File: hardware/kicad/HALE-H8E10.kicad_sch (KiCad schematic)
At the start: 11 parts, among them U1001 74AHCT1G125, U1002 XIAO-ESP32-S3-Plus-SMD

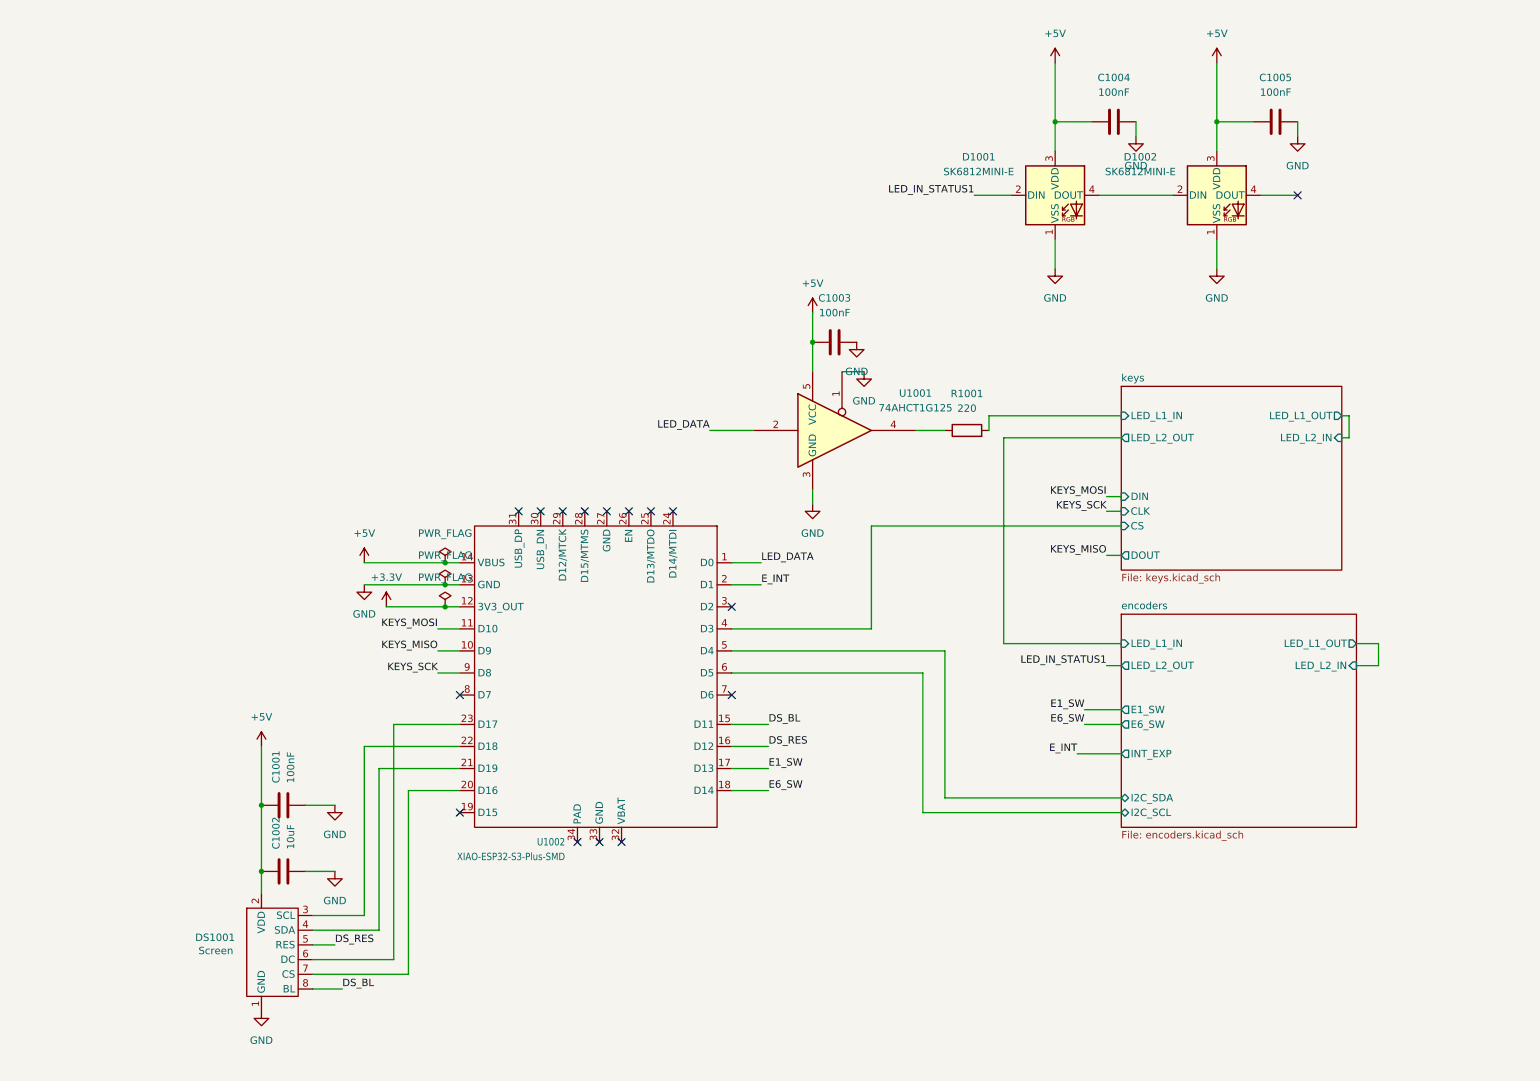
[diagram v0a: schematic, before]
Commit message: WIP checkpoint commit before spliting the 5V rail
hardware/kicad/HALE-H8E10.kicad_pcb: Manufacturing: changed the board
  outline; tenting front back → -; covering - → -; plugging - → -;
  capping - → no; filling - → no; changed the plot output settings.
  Gergő Törcsvári: updated from the schematic (added C1003, C1004,
  C2001-C2016, C3001, C3002, C21001 and 83 more, TP1001-TP1003 not
  placed yet); placed C1003, C1004, C2001-C2016, C3001, C3002, C21001
  and 82 more; routed D_CS, DS_BL, DS_RES, E_INT and 86 more nets; added
  a zone on F.Cu, B.Cu; added a zone on F.Cu, B.Cu; added a zone on
  F.Cu, B.Cu; added a zone on F.Cu, B.Cu; and 15 more changes.
hardware/kicad/HALE-H8E10.kicad_pro: Manufacturing: max arc error - →
  0.005 mm; min connection width - → 0 mm; min groove width - → 0 mm;
  min microvia diameter - → 0.2 mm; min microvia drill - → 0.1 mm; min
  resolved spokes - → 2 mm; solder mask to copper clearance - → 0 mm;
  use height for length calcs - → true mm. Gergő Törcsvári: changed the
  predefined track widths (+4); changed the predefined diff pair sizes
  (+1); changed teardrop settings; changed default text and line
  settings; changed 62 DRC rule severities; changed DRC exclusions;
  changed schematic settings; changed 19 board.design settings settings.
hardware/kicad/HALE-H8E10.kicad_sch: Gergő Törcsvári added R1002, R1003
  and TP1001-TP1003 and wired them; removed C1001, C1002, C1005, D1001
  and D1002; changed C1004 value 100nF → 10uF; changed C1004 footprint
  Capacitor_SMD:C_0603_1608Metric_Pad1.08x0.95mm_HandSolder →
  Capacitor_SMD:C_0805_2012Metric_Pad1.18x1.45mm_HandSolder; changed
  C1004 LCSC C14663 → C15850; changed C1004 wiring (pins 1 and 2 now on
  GND and +5V); changed DS1001 wiring (pin 7 now on /D_CS); and 4 more
  changes.
hardware/kicad/encoders.kicad_sch: Gergő Törcsvári changed U3001 wiring;
  changed U3002 wiring; rearranged the sheet.
hardware/kicad/keys.kicad_sch: Gergő Törcsvári added TP2001 (3V3A) and
  wired it; change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
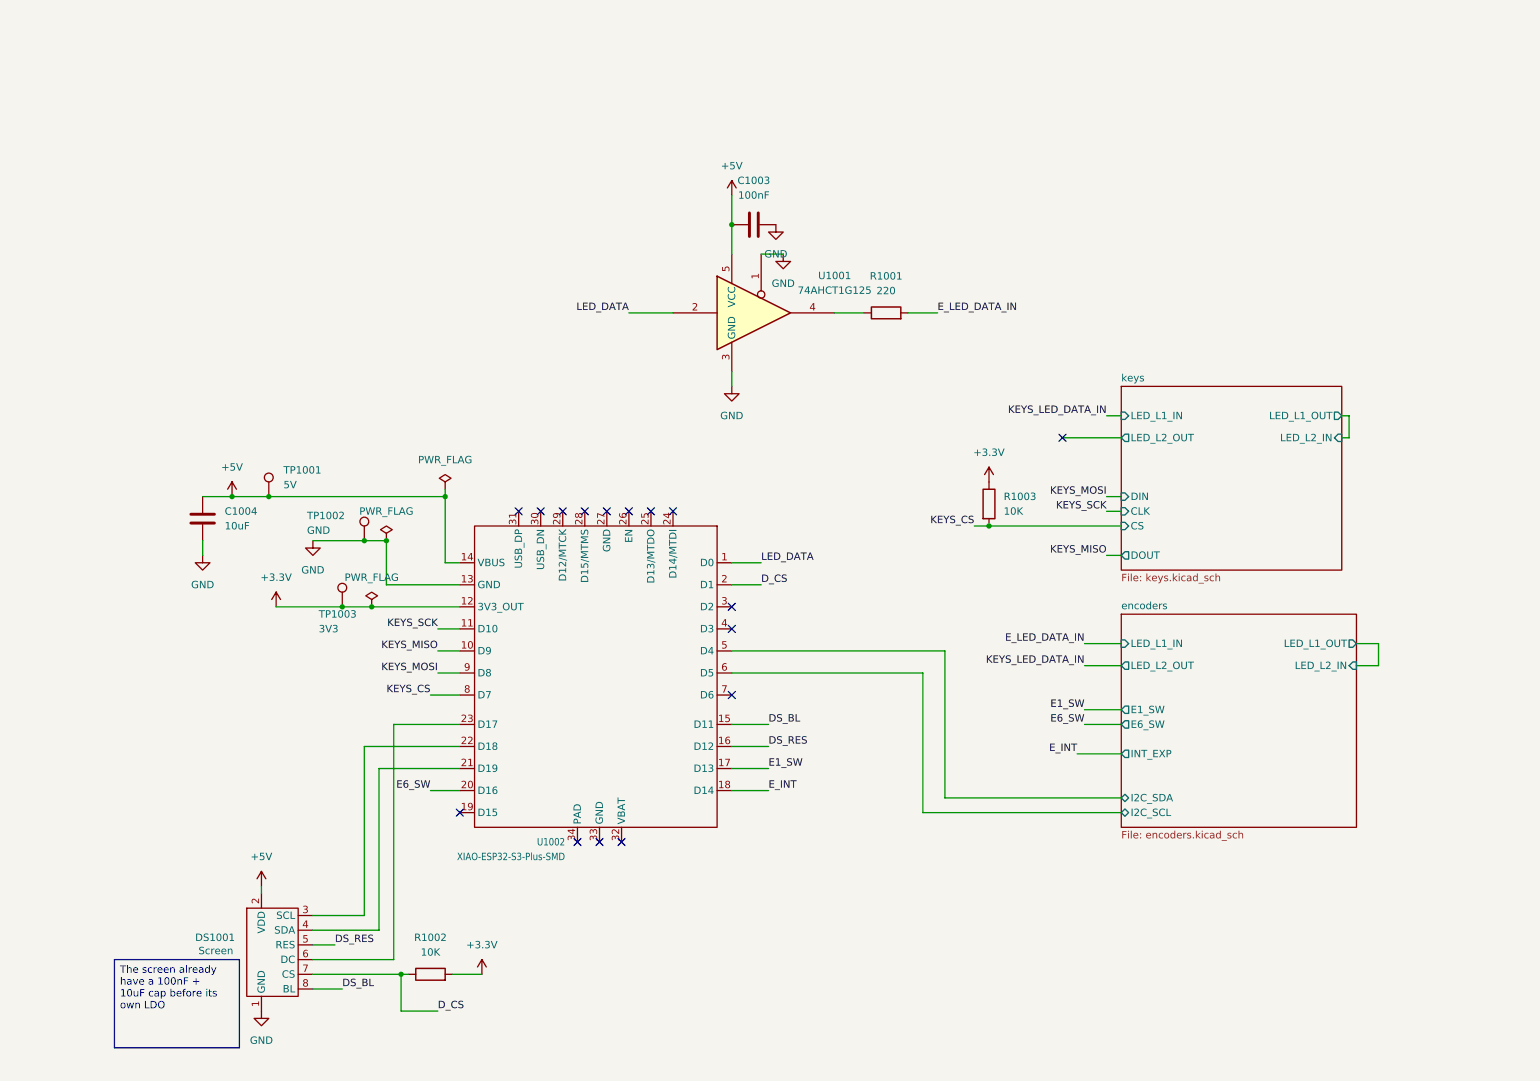
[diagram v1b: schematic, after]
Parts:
- removed C1001, C1005: 100nF, Capacitor_SMD:C_0603_1608Metric_Pad1.08x0.95mm_HandSolder, symbol Device:C
- removed C1002: 10uF, Capacitor_SMD:C_0805_2012Metric_Pad1.18x1.45mm_HandSolder, symbol Device:C
- removed D1001, D1002: SK6812MINI-E, LED_SMD:LED_SK6812MINI-E_3.2x2.8mm_P1.5mm_ReverseMount, symbol LED:SK6812MINI-E
- added R1002, R1003: 10K, Resistor_SMD:R_0603_1608Metric_Pad0.98x0.95mm_HandSolder, symbol Device:R
- added TP1001: 5V, TestPoint:TestPoint_Pad_D2.0mm, symbol Connector:TestPoint
- added TP1002: GND, TestPoint:TestPoint_Pad_D2.0mm, symbol Connector:TestPoint
- added TP1003: 3V3, TestPoint:TestPoint_Pad_D2.0mm, symbol Connector:TestPoint
- C1004: value 100nF -> 10uF; footprint Capacitor_SMD:C_0603_1608Metric_Pad1.08x0.95mm_HandSolder -> Capacitor_SMD:C_0805_2012Metric_Pad1.18x1.45mm_HandSolder; LCSC C14663 -> C15850
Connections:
- net +3.3V: now also R1002.2, R1003.1, TP1003.1
- net +5V: now also C1004.2, TP1001.1; no longer C1004.1
- net E6_SW: now also U1002.20 (D16); no longer U1002.18 (D14)
- net E_INT: now also U1002.18 (D14); no longer U1002.2 (D1)
- net GND: now also C1004.1, TP1002.1; no longer C1004.2
- net KEYS_MOSI: now also U1002.9 (D8); no longer U1002.11 (D10)
- net KEYS_SCK: now also U1002.11 (D10); no longer U1002.9 (D8)
- net D_CS: now reaches DS1001.7 (CS)
- net D_CS: now also U1002.2 (D1), R1002.1; no longer U1002.20 (D16)
- net KEYS_CS: now reaches U1002.8 (D7)
- net KEYS_CS: now also R1003.2
- net keys/CS: no longer names the net of U1002.4 (D3)
- net keys/LED_L1_IN renamed E_LED_DATA_IN
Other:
- moved on the sheet: C1003, R1001, U1001

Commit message: "finished" PCB
hardware/kicad/HALE-H8E10.kicad_pcb: Manufacturing: changed the board
  outline. Gergő Törcsvári: updated from the schematic (added C1001,
  C1002, C1004-C1009, H1001-H1012, R1004, R1005 and 5 more; removed
  R1002 and R1003; nets changed on 44 pads); placed C1001, C1002,
  C1004-C1009, H1001-H1012, R1004, R1005 and 4 more; added REF**;
  removed C1004; moved C1003, C2002, C2003, C2006, R1001, TP2001 and
  U1001; routed EN_AUX, EN_LED, +5V_AUX, +5V_LED and 3 more nets;
  rerouted D_CS, DS_BL, DS_RES, E_INT and 21 more nets; and 3 more
  changes.
hardware/kicad/HALE-H8E10.kicad_pro: Gergő Törcsvári excluded 2 DRC
  violations; changed schematic settings.
hardware/kicad/HALE-H8E10.kicad_sch: Gergő Törcsvári added C1001, C1002,
  C1005-C1009, H1001-H1012, R1004, R1005 and 4 more and wired them;
  removed R1002 and R1003; changed 4 parts' fields; changed C1004 wiring
  (pin 1 now on +5V); renamed net unconnected-(U1002-D3-Pad4) to
  /EN_AUX; renamed net unconnected-(U1002-D15-Pad19) to /EN_LED; split
  +5V into +5V_AUX and +5V_LED; and 4 more changes.
hardware/kicad/encoder.kicad_sch: Gergő Törcsvári changed 10 parts'
  fields; renamed net unconnected-(U1002-D3-Pad4) to /EN_AUX; renamed
  net unconnected-(U1002-D15-Pad19) to /EN_LED; split +5V into +5V_AUX
  and +5V_LED.
hardware/kicad/encoders.kicad_sch: Gergő Törcsvári changed 6 parts'
  fields; renamed net unconnected-(U1002-D3-Pad4) to /EN_AUX; renamed
  net unconnected-(U1002-D15-Pad19) to /EN_LED; split +5V into +5V_AUX
  and +5V_LED.
hardware/kicad/key_cell.kicad_sch: Gergő Törcsvári changed 16 parts'
  fields; renamed net unconnected-(U1002-D3-Pad4) to /EN_AUX; renamed
  net unconnected-(U1002-D15-Pad19) to /EN_LED; split +5V into +5V_AUX
  and +5V_LED.
hardware/kicad/keys.kicad_sch: Gergő Törcsvári added R2001 (10K) and
  wired it to /KEYS_CS; changed 6 parts' fields; renamed net
  unconnected-(U1002-D3-Pad4) to /EN_AUX; renamed net
  unconnected-(U1002-D15-Pad19) to /EN_LED; split +5V into +5V_A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
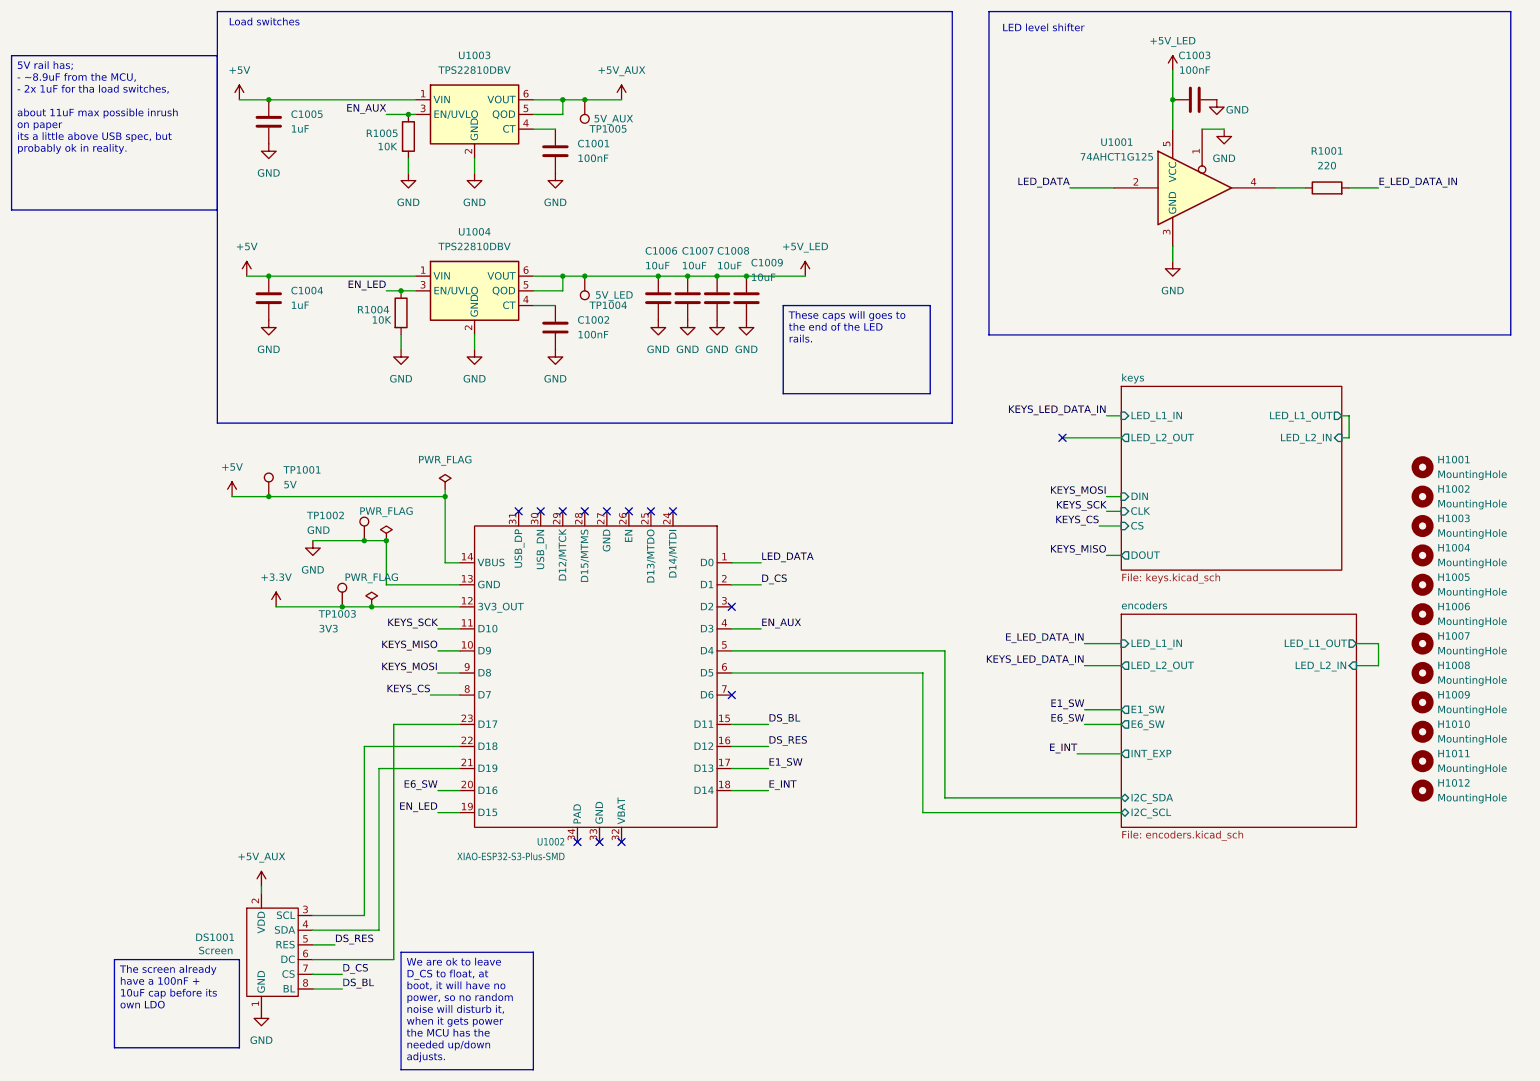
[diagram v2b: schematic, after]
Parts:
- removed R1002, R1003: 10K, Resistor_SMD:R_0603_1608Metric_Pad0.98x0.95mm_HandSolder, symbol Device:R
- added C1001, C1002: 100nF, Capacitor_SMD:C_0603_1608Metric_Pad1.08x0.95mm_HandSolder, symbol Device:C
- added C1005: 1uF, Capacitor_SMD:C_0603_1608Metric_Pad1.08x0.95mm_HandSolder, symbol Device:C
- added C1006, C1007, C1008, C1009: 10uF, Capacitor_SMD:C_0805_2012Metric_Pad1.18x1.45mm_HandSolder, symbol Device:C
- added H1001, H1002, H1003, H1004, H1005, H1006, H1007, H1008, H1009, H1010, H1011, H1012: MountingHole, MountingHole:MountingHole_2.2mm_M2, symbol Mechanical:MountingHole
- added R1004, R1005: 10K, Resistor_SMD:R_0603_1608Metric_Pad0.98x0.95mm_HandSolder, symbol Device:R
- added TP1004: 5V_LED, TestPoint:TestPoint_Pad_D2.0mm, symbol Connector:TestPoint
- added TP1005: 5V_AUX, TestPoint:TestPoint_Pad_D2.0mm, symbol Connector:TestPoint
- added U1003, U1004: TPS22810DBV, Package_TO_SOT_SMD:SOT-23-6, symbol Power_Management:TPS22810DBV
- C1004: value 10uF -> 1uF; footprint Capacitor_SMD:C_0805_2012Metric_Pad1.18x1.45mm_HandSolder -> Capacitor_SMD:C_0603_1608Metric_Pad1.08x0.95mm_HandSolder; LCSC C15850 -> C15849
- R1001: LCSC (none) -> C22962
- U1001: LCSC (none) -> C7484
- U1002: LCSC (none) -> C47997983
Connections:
- net +5V: now also C1004.1, C1005.1, U1003.1 (VIN), U1004.1 (VIN); no longer C1003.2, C1004.2, DS1001.2 (VDD), U1001.5 (VCC)
- net GND: now also C1004.2, C1001.2, C1002.2, C1005.2, C1006.2, C1007.2, C1008.2, C1009.2, R1004.2, R1005.2, U1003.2 (GND), U1004.2 (GND); no longer C1004.1
- net EN_LED: now reaches U1002.19 (D15)
- net EN_LED: now also R1004.1, U1004.3 (EN/UVLO)
- net EN_AUX: now reaches U1002.4 (D3)
- net EN_AUX: now also R1005.1, U1003.3 (EN/UVLO)
- new net: C1001.1, U1003.4 (CT)
- new net: C1002.1, U1004.4 (CT)
- new net +5V_AUX: DS1001.2 (VDD), TP1005.1, U1003.5 (QOD), U1003.6 (VOUT)
- new net +5V_LED: C1003.2, C1006.1, C1007.1, C1008.1, C1009.1, TP1004.1, U1001.5 (VCC), U1004.5 (QOD), U1004.6 (VOUT)
- no-connect marks 16 -> 14
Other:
- note added: "LED level shifter"
- note added: "Load switches"
- moved on the sheet: C1003, R1001, U1001
